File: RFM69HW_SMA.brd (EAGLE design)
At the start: 25.4 x 40.6 mm, 19 parts, among them U1 RFM69W, U2 MCP1701, X1 ANT

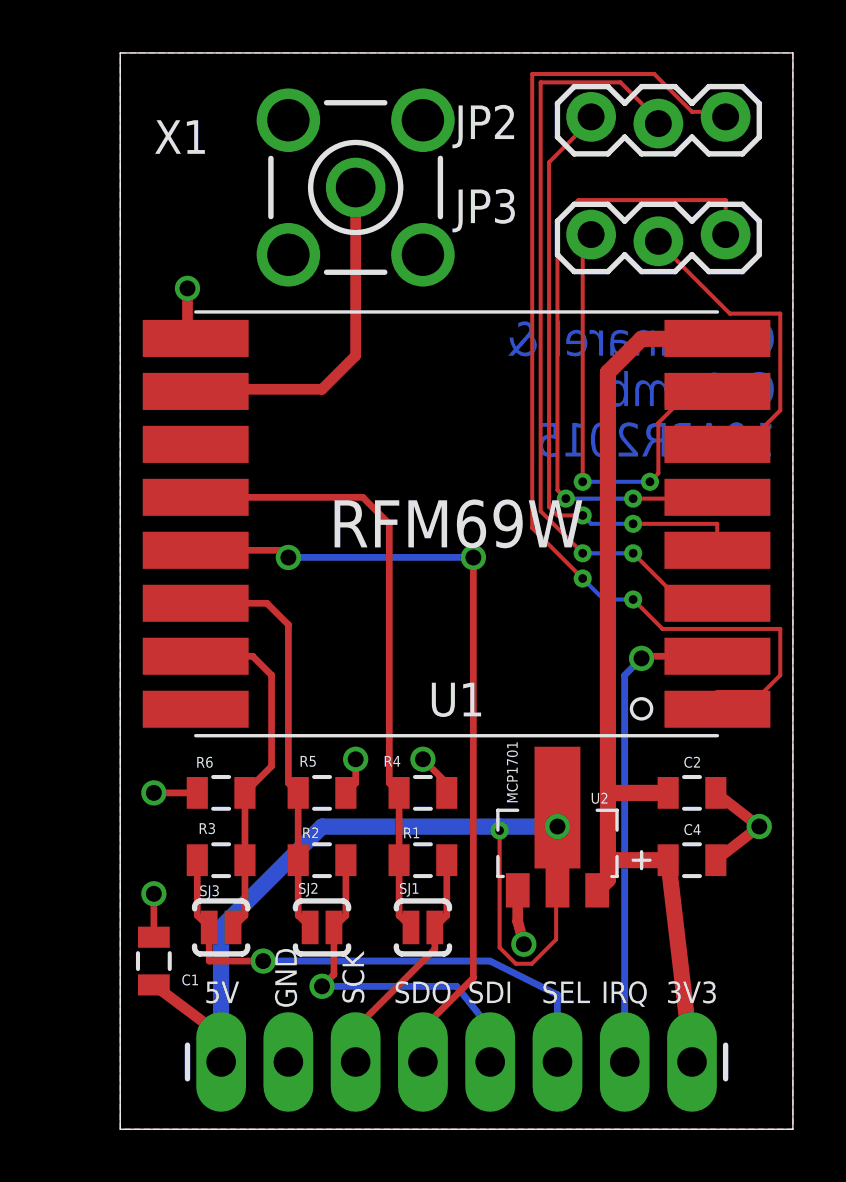
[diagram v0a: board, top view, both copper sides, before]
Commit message: Slight relayout
Re-layout. Break out all I/O pins. Use RFM69HW variant (same pinout).
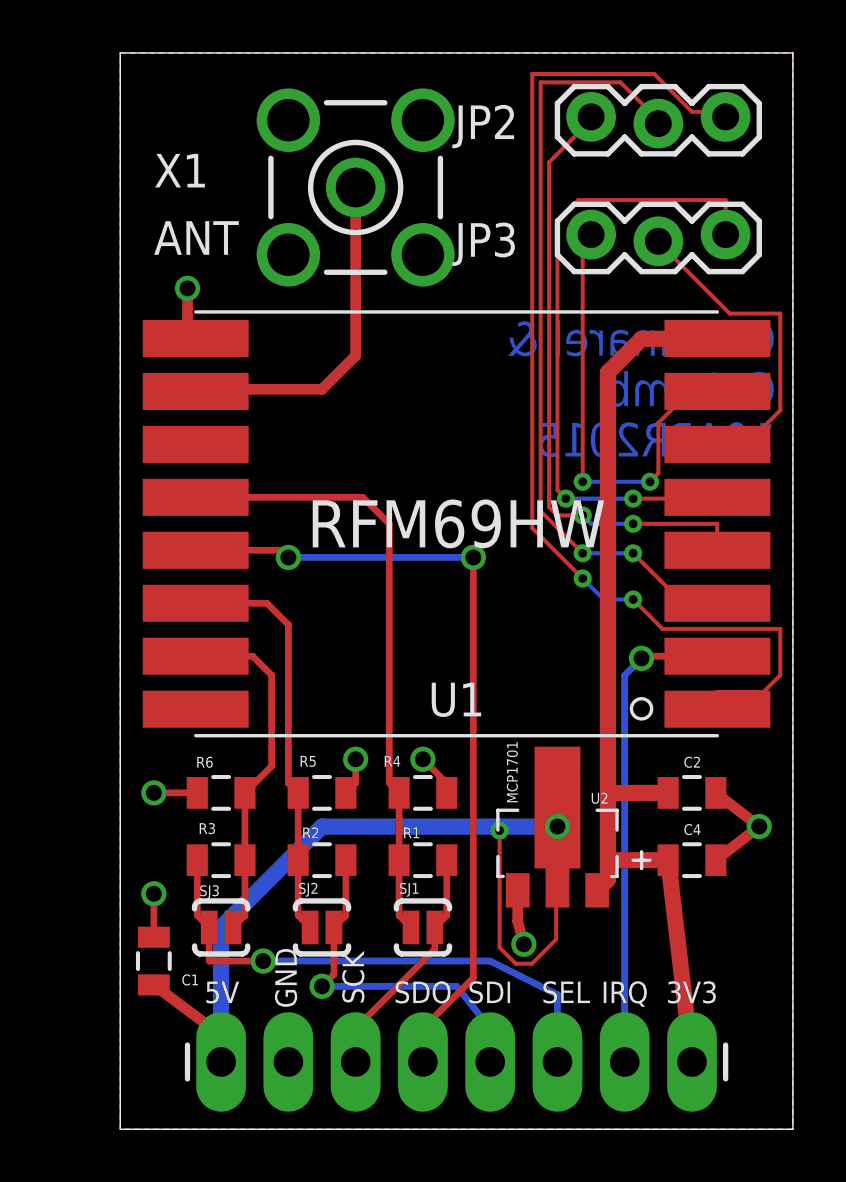
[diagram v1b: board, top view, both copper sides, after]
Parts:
- U1: value RFM69W -> RFM69HW; device ChipsParts:RFM69W -> custom_parts:RFM69
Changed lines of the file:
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@@
 <elements>
 <element name="FRAME1" library="SparkFun-Aesthetics" package="CREATIVE_COMMONS" value="FRAME-LETTER" x="17.78" y="-8.89"/>
-<element name="U1" library="ChipsParts" package="RFM69W" value="RFM69W" x="12.7" y="22.86" rot="R180"/>
+<element name="U1" library="custom_parts" package="RFM69" value="RFM69HW" x="12.7" y="22.86" rot="R180"/>
 <element name="U2" library="ChipsParts" package="SOT-89" value="MCP1701" x="16.51" y="10.795"/>
 <element name="JP1" library="SparkFun-Connectors" package="1X08_LONGPADS" value="" x="3.81" y="2.54" smashed="yes">
@@
 <attribute name="MF" value="TE Connectivity" x="8.89" y="35.56" size="1.778" layer="27" display="off"/>
 <attribute name="OC_DIGIKEY" value="A97594-ND" x="8.89" y="35.56" size="1.778" layer="27" display="off"/>
-<attribute name="NAME" x="1.27" y="36.83" size="1.27" layer="25"/>
-<attribute name="VALUE" x="1.27" y="34.29" size="1.27" layer="27"/>
+<attribute name="NAME" x="1.27" y="35.56" size="1.27" layer="25"/>
+<attribute name="VALUE" x="1.27" y="33.02" size="1.27" layer="25"/>
 </element>
 <element name="JP2" library="SparkFun-Connectors" package="1X03_LOCK" value="" x="17.78" y="38.1" smashed="yes">
@@
 </element>
 <element name="JP3" library="SparkFun-Connectors" package="1X03_LOCK" value="" x="17.78" y="33.655" smashed="yes">
-<attribute name="NAME" x="12.6238" y="34.2138" size="1.27" layer="25" ratio="10"/>
+<attribute name="NAME" x="12.6238" y="32.9438" size="1.27" layer="25" ratio="10"/>
 <attribute name="VALUE" x="16.51" y="30.48" size="1.27" layer="27"/>
 </element>

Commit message: Update to remove JP2 and JP3
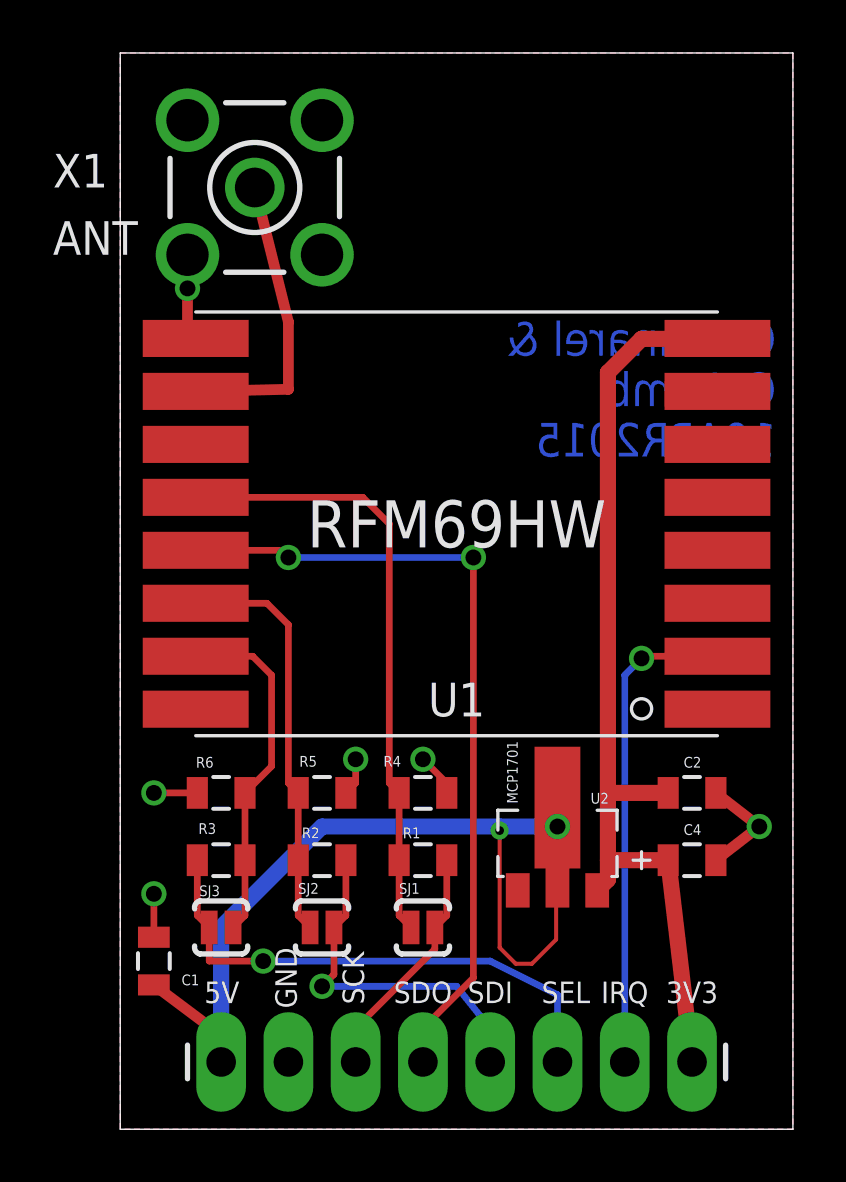
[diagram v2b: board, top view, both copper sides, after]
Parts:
- removed JP2, JP3: (no value), SparkFun-Connectors:1X03_LOCK
- moved X1 3.81 mm to (5.08, 35.6)
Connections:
- removed net N$12: JP2.3, U1.1
- removed net N$13: JP2.2, U1.3
- removed net N$14: JP2.1, U1.4
- removed net N$15: JP3.1, U1.7
- removed net N$16: JP3.2, U1.6
- removed net N$17: JP3.3, U1.5
- net GND: no longer U2.1
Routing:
- net N$12: track 41.9 -> 0.00 mm, vias 2 -> 0
- net N$13: track 30.8 -> 0.00 mm, vias 2 -> 0
- net N$17: track 24.4 -> 0.00 mm, vias 2 -> 0
- net N$14: track 23.0 -> 0.00 mm, vias 2 -> 0
- net N$15: track 19.1 -> 0.00 mm, vias 2 -> 0
- net N$16: track 13.4 -> 0.00 mm
- net GND: track 14.6 -> 12.5 mm, vias 7 -> 6
- net N$11: track 14.0 -> 12.4 mm
